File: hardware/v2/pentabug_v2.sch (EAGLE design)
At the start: 49 parts, among them IC1 ATMEGA88

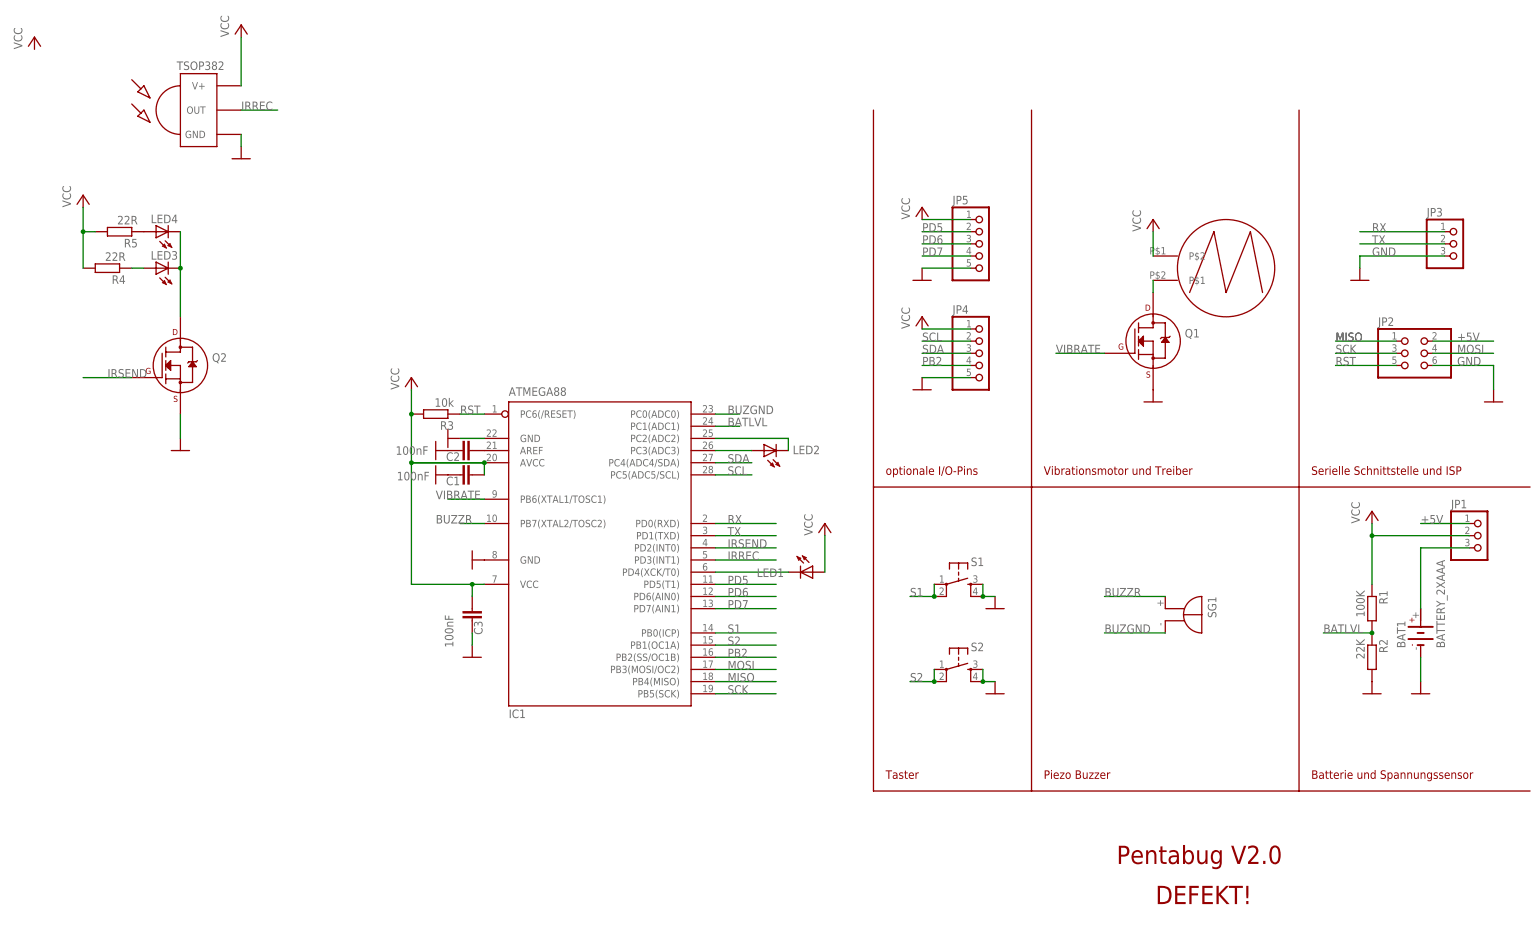
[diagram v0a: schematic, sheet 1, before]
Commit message: fixes issue #6, correct values for r4 and r5
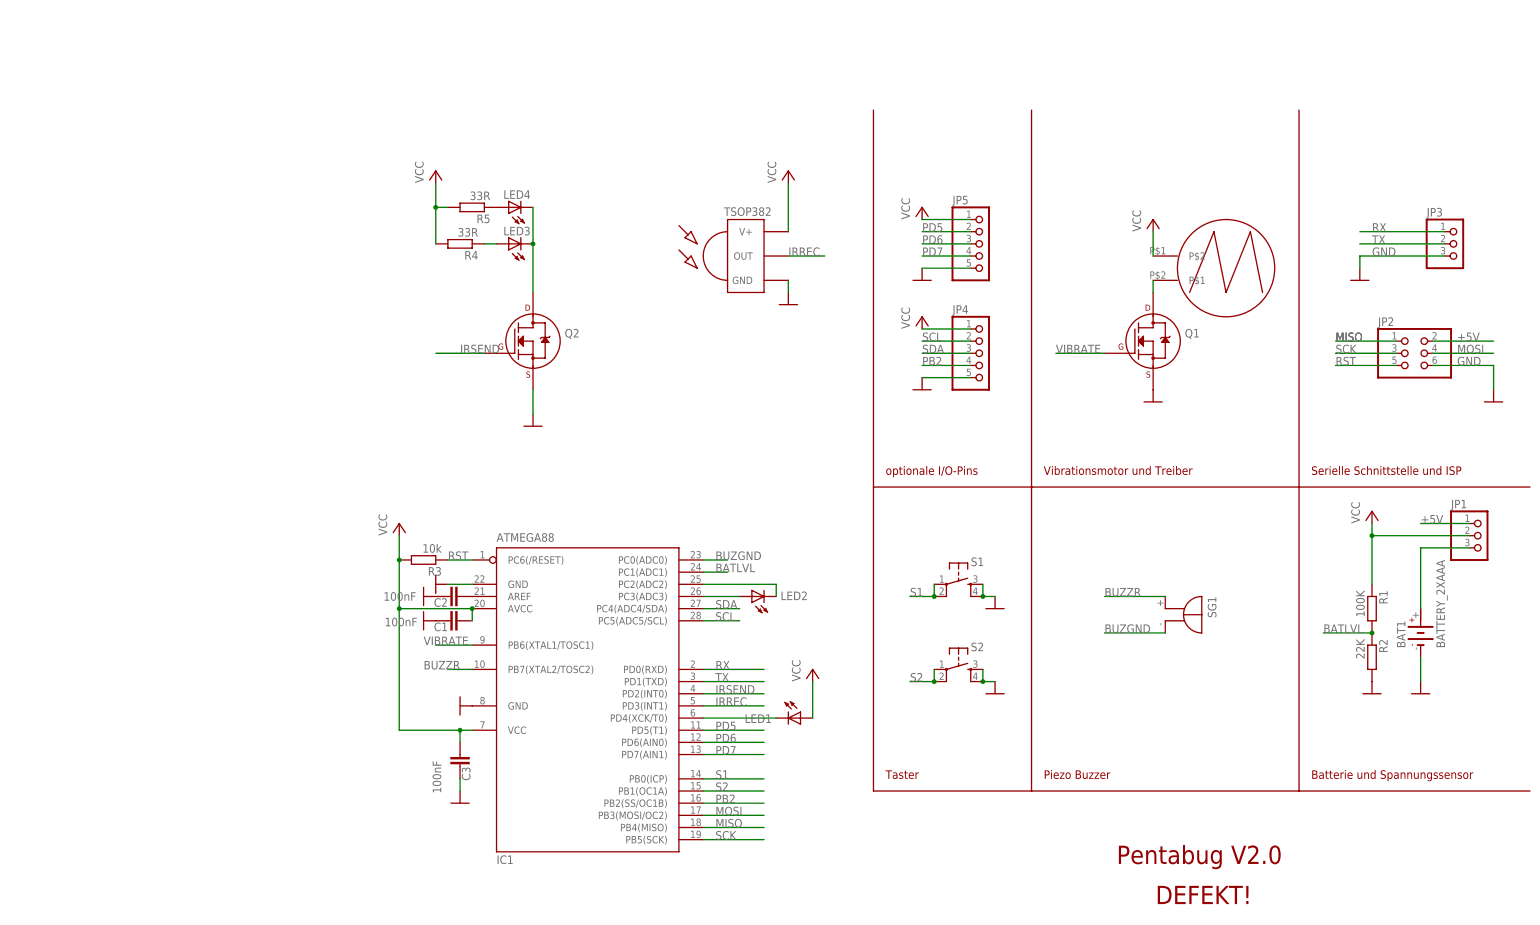
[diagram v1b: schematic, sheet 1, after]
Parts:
- R4, R5: value 22R -> 33R
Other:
- moved on the sheet: C1, C2, C3, IC1, LED1, LED2, LED3, LED4, Q2, R3, R4, R5

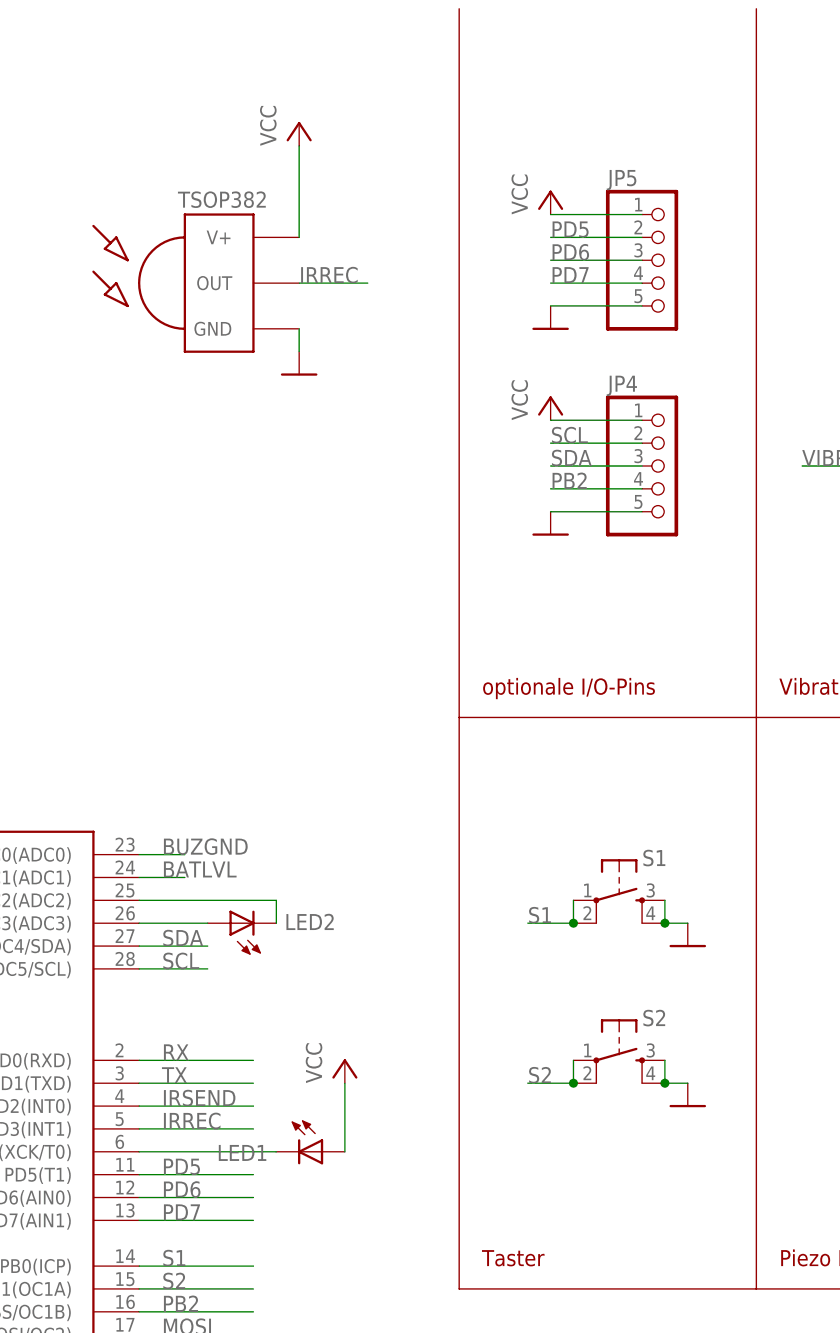
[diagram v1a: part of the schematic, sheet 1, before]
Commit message: correct labels in schematic for pentatonic fixes #7
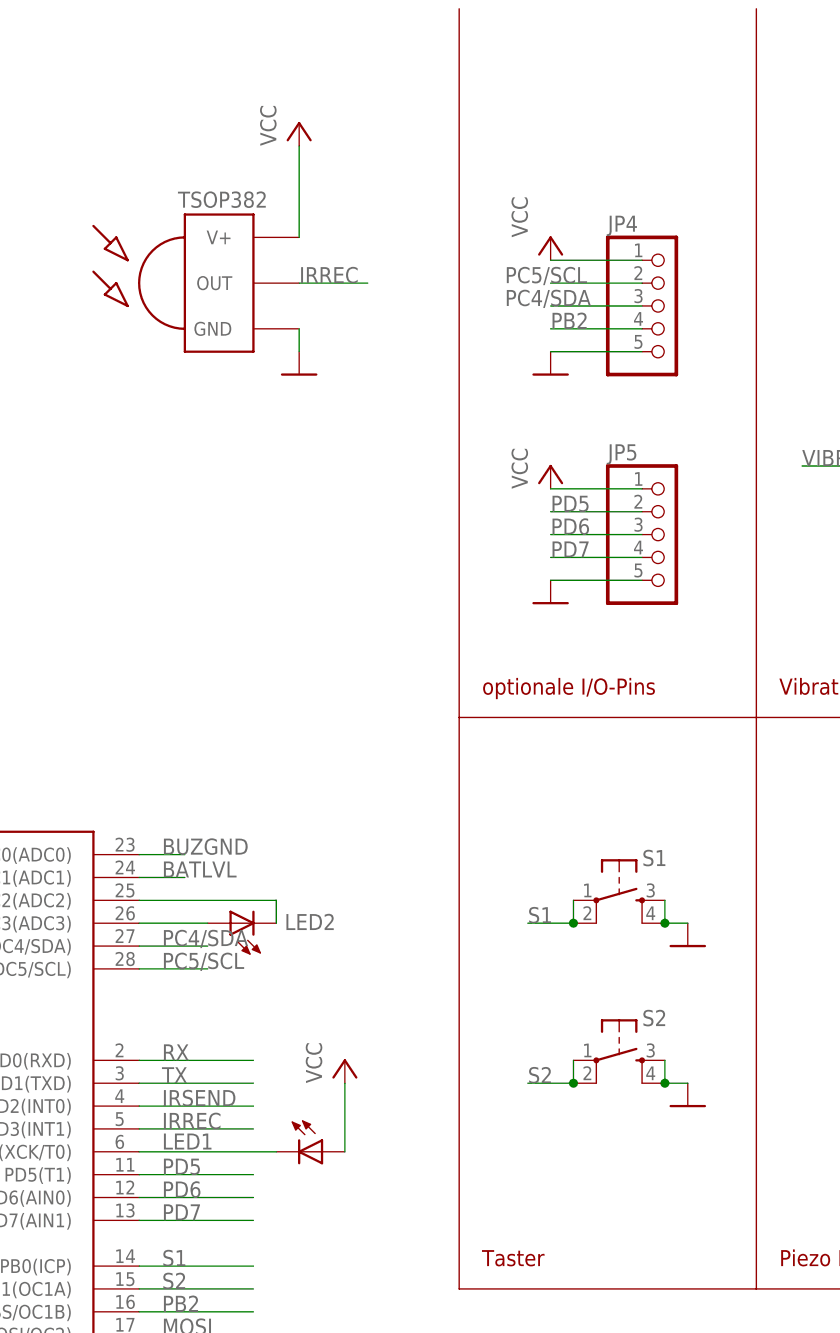
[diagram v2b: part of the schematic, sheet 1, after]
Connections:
- net PB2_T renamed PD7_T
- net SCL renamed PC5/SCL
- net SDA renamed PC4/SDA
- net PC4_T: now also LED9.C, S7.S, S7.S1, SV5.3; no longer LED6.C, S4.S, S4.S1, SV4.3
- net PC5_T: now also LED8.C, S6.S, S6.S1, SV5.2; no longer LED5.C, S3.S, S3.S1, SV4.2
- net PD5_T: now also LED5.C, S3.S, S3.S1, SV4.2; no longer LED8.C, S6.S, S6.S1, SV5.2
- net PD6_T: now also LED6.C, S4.S, S4.S1, SV4.3; no longer LED9.C, S7.S, S7.S1, SV5.3
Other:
- moved on the sheet: JP4, JP5, SV4, SV5
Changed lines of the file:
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@@
 <?xml version="1.0" encoding="utf-8"?>
 <!DOCTYPE eagle SYSTEM "eagle.dtd">
-<eagle version="6.4">
+<eagle version="6.5.0">
 <drawing>
 <settings>
@@
 <instance part="R3" gate="G$1" x="-25.4" y="25.4" rot="R180"/>
 <instance part="LED1" gate="G$1" x="53.34" y="-7.62" smashed="yes" rot="R270">
-<attribute name="NAME" x="41.656" y="-8.636" size="1.778" layer="95"/>
+<attribute name="NAME" x="35.56" y="-7.366" size="1.778" layer="95"/>
 <attribute name="VALUE" x="48.768" y="-13.335" size="1.778" layer="96"/>
 </instance>
@@
 <instance part="R2" gate="G$1" x="172.72" y="5.08" rot="R270"/>
 <instance part="GND13" gate="1" x="172.72" y="-2.54" smashed="yes"/>
-<instance part="JP5" gate="A" x="91.44" y="91.44"/>
-<instance part="JP4" gate="A" x="91.44" y="68.58"/>
-<instance part="GND14" gate="1" x="78.74" y="60.96" smashed="yes"/>
-<instance part="GND15" gate="1" x="78.74" y="83.82" smashed="yes"/>
-<instance part="P+4" gate="VCC" x="78.74" y="76.2"/>
-<instance part="P+6" gate="VCC" x="78.74" y="99.06"/>
+<instance part="JP5" gate="A" x="91.44" y="60.96"/>
+<instance part="JP4" gate="A" x="91.44" y="86.36"/>
+<instance part="GND14" gate="1" x="78.74" y="78.74" smashed="yes"/>
+<instance part="GND15" gate="1" x="78.74" y="53.34" smashed="yes"/>
+<instance part="P+4" gate="VCC" x="78.74" y="93.98" smashed="yes">
+<attribute name="VALUE" x="76.2" y="93.98" size="1.778" layer="96" rot="R90"/>
+</instance>
+<instance part="P+6" gate="VCC" x="78.74" y="68.58" smashed="yes">
+<attribute name="VALUE" x="76.2" y="66.04" size="1.778" layer="96" rot="R90"/>
+</instance>
 <instance part="JP1" gate="A" x="195.58" y="30.48"/>
 <instance part="Q2" gate="G$1" x="-2.54" y="71.12"/>
@@
 <segment>
 <pinref part="JP5" gate="A" pin="2"/>
-<wire x1="88.9" y1="93.98" x2="78.74" y2="93.98" width="0.1524" layer="91"/>
-<label x="78.74" y="93.98" size="1.778" layer="95"/>
+<wire x1="88.9" y1="63.5" x2="78.74" y2="63.5" width="0.1524" layer="91"/>
+<label x="78.74" y="63.5" size="1.778" layer="95"/>
 </segment>
 </net>
@@
 <pinref part="JP4" gate="A" pin="1"/>
 <pinref part="P+4" gate="VCC" pin="VCC"/>
-<wire x1="78.74" y1="73.66" x2="88.9" y2="73.66" width="0.1524" layer="91"/>
+<wire x1="78.74" y1="91.44" x2="88.9" y2="91.44" width="0.1524" layer="91"/>
 </segment>
 <segment>
 <pinref part="JP5" gate="A" pin="1"/>
 <pinref part="P+6" gate="VCC" pin="VCC"/>
-<wire x1="78.74" y1="96.52" x2="88.9" y2="96.52" width="0.1524" layer="91"/>
+<wire x1="78.74" y1="66.04" x2="88.9" y2="66.04" width="0.1524" layer="91"/>
 </segment>
 <segment>
@@
 <pinref part="JP5" gate="A" pin="5"/>
 <pinref part="GND15" gate="1" pin="GND"/>
-<wire x1="78.74" y1="86.36" x2="88.9" y2="86.36" width="0.1524" layer="91"/>
+<wire x1="78.74" y1="55.88" x2="88.9" y2="55.88" width="0.1524" layer="91"/>
 </segment>
 <segment>
@@
 <pinref part="JP4" gate="A" pin="5"/>
 <pinref part="GND14" gate="1" pin="GND"/>
-<wire x1="78.74" y1="63.5" x2="88.9" y2="63.5" width="0.1524" layer="91"/>
+<wire x1="78.74" y1="81.28" x2="88.9" y2="81.28" width="0.1524" layer="91"/>
 </segment>
 </net>
@@
 <segment>
 <pinref part="JP5" gate="A" pin="3"/>
-<wire x1="88.9" y1="91.44" x2="78.74" y2="91.44" width="0.1524" layer="91"/>
-<label x="78.74" y="91.44" size="1.778" layer="95"/>
+<wire x1="88.9" y1="60.96" x2="78.74" y2="60.96" width="0.1524" layer="91"/>
+<label x="78.74" y="60.96" size="1.778" layer="95"/>
 </segment>
 </net>
@@
 </segment>
 </net>
-<net name="SCL" class="0">
+<net name="PC5/SCL" class="0">
 <segment>
 <pinref part="JP4" gate="A" pin="2"/>
-<wire x1="88.9" y1="71.12" x2="78.74" y2="71.12" width="0.1524" layer="91"/>
-<label x="78.74" y="71.12" size="1.778" layer="95"/>
+<wire x1="88.9" y1="88.9" x2="78.74" y2="88.9" width="0.1524" layer="91"/>
+<label x="73.66" y="88.9" size="1.778" layer="95"/>
 </segment>
 <segment>
@@
 </segment>
 </net>
-<net name="SDA" class="0">
+<net name="PC4/SDA" class="0">
 <segment>
 <pinref part="JP4" gate="A" pin="3"/>
-<wire x1="88.9" y1="68.58" x2="78.74" y2="68.58" width="0.1524" layer="91"/>
-<label x="78.74" y="68.58" size="1.778" layer="95"/>
+<wire x1="88.9" y1="86.36" x2="78.74" y2="86.36" width="0.1524" layer="91"/>
+<label x="73.66" y="86.36" size="1.778" layer="95"/>
 </segment>
 <segment>
@@
 <segment>
 <pinref part="JP4" gate="A" pin="4"/>
-<wire x1="88.9" y1="66.04" x2="78.74" y2="66.04" width="0.1524" layer="91"/>
-<label x="78.74" y="66.04" size="1.778" layer="95"/>
+<wire x1="88.9" y1="83.82" x2="78.74" y2="83.82" width="0.1524" layer="91"/>
+<label x="78.74" y="83.82" size="1.778" layer="95"/>
 </segment>
 </net>
@@
 <segment>
 <pinref part="JP5" gate="A" pin="4"/>
-<wire x1="88.9" y1="88.9" x2="78.74" y2="88.9" width="0.1524" layer="91"/>
-<label x="78.74" y="88.9" size="1.778" layer="95"/>
+<wire x1="88.9" y1="58.42" x2="78.74" y2="58.42" width="0.1524" layer="91"/>
+<label x="78.74" y="58.42" size="1.778" layer="95"/>
 </segment>
 </net>
@@
 </plain>
 <instances>
-<instance part="SV4" gate="G$1" x="35.56" y="63.5" rot="MR180"/>
-<instance part="SV5" gate="G$1" x="35.56" y="27.94" rot="MR180"/>
-<instance part="P+11" gate="VCC" x="43.18" y="35.56"/>
-<instance part="GND17" gate="1" x="50.8" y="55.88"/>
-<instance part="GND18" gate="1" x="48.26" y="20.32"/>
+<instance part="SV4" gate="G$1" x="35.56" y="33.02" rot="MR180"/>
+<instance part="SV5" gate="G$1" x="35.56" y="63.5" rot="MR180"/>
+<instance part="P+11" gate="VCC" x="48.26" y="71.12"/>
+<instance part="GND17" gate="1" x="50.8" y="25.4"/>
+<instance part="GND18" gate="1" x="48.26" y="55.88"/>
 <instance part="LED5" gate="G$1" x="81.28" y="58.42"/>
 <instance part="S3" gate="1" x="78.74" y="43.18"/>
@@
 <pinref part="SV5" gate="G$1" pin="1"/>
 <pinref part="P+11" gate="VCC" pin="VCC"/>
+<wire x1="48.26" y1="68.58" x2="43.18" y2="68.58" width="0.1524" layer="91"/>
 </segment>
 <segment>
@@
 <pinref part="SV4" gate="G$1" pin="5"/>
 <pinref part="GND17" gate="1" pin="GND"/>
-<wire x1="50.8" y1="58.42" x2="43.18" y2="58.42" width="0.1524" layer="91"/>
+<wire x1="50.8" y1="27.94" x2="43.18" y2="27.94" width="0.1524" layer="91"/>
 </segment>
 <segment>
 <pinref part="SV5" gate="G$1" pin="5"/>
 <pinref part="GND18" gate="1" pin="GND"/>
-<wire x1="48.26" y1="22.86" x2="43.18" y2="22.86" width="0.1524" layer="91"/>
+<wire x1="48.26" y1="58.42" x2="43.18" y2="58.42" width="0.1524" layer="91"/>
 </segment>
 <segment>
@@
 </segment>
 </net>
-<net name="PC5_T" class="0">
+<net name="PD5_T" class="0">
 <segment>
 <pinref part="SV4" gate="G$1" pin="2"/>
-<wire x1="43.18" y1="66.04" x2="53.34" y2="66.04" width="0.1524" layer="91"/>
-<label x="48.26" y="66.04" size="1.778" layer="95"/>
+<wire x1="43.18" y1="35.56" x2="53.34" y2="35.56" width="0.1524" layer="91"/>
+<label x="48.26" y="35.56" size="1.778" layer="95"/>
 </segment>
 <segment>
@@
 </segment>
 </net>
-<net name="PC4_T" class="0">
+<net name="PD6_T" class="0">
 <segment>
 <pinref part="SV4" gate="G$1" pin="3"/>
-<wire x1="43.18" y1="63.5" x2="53.34" y2="63.5" width="0.1524" layer="91"/>
-<label x="48.26" y="63.5" size="1.778" layer="95"/>
+<wire x1="43.18" y1="33.02" x2="53.34" y2="33.02" width="0.1524" layer="91"/>
+<label x="48.26" y="33.02" size="1.778" layer="95"/>
 </segment>
 <segment>
@@
 </segment>
 </net>
-<net name="PD5_T" class="0">
+<net name="PC5_T" class="0">
 <segment>
 <pinref part="SV5" gate="G$1" pin="2"/>
-<wire x1="43.18" y1="30.48" x2="53.34" y2="30.48" width="0.1524" layer="91"/>
-<label x="48.26" y="30.48" size="1.778" layer="95"/>
+<wire x1="43.18" y1="66.04" x2="53.34" y2="66.04" width="0.1524" layer="91"/>
+<label x="48.26" y="66.04" size="1.778" layer="95"/>
 </segment>
 <segment>
@@
 </segment>
 </net>
-<net name="PD6_T" class="0">
+<net name="PC4_T" class="0">
 <segment>
 <pinref part="SV5" gate="G$1" pin="3"/>
-<wire x1="43.18" y1="27.94" x2="53.34" y2="27.94" width="0.1524" layer="91"/>
-<label x="48.26" y="27.94" size="1.778" layer="95"/>
+<wire x1="43.18" y1="63.5" x2="53.34" y2="63.5" width="0.1524" layer="91"/>
+<label x="48.26" y="63.5" size="1.778" layer="95"/>
 </segment>
 <segment>
@@
 </segment>
 </net>
-<net name="PB2_T" class="0">
+<net name="PD7_T" class="0">
 <segment>
 <pinref part="SV4" gate="G$1" pin="4"/>
-<wire x1="43.18" y1="60.96" x2="53.34" y2="60.96" width="0.1524" layer="91"/>
-<label x="48.26" y="60.96" size="1.778" layer="95"/>
-</segment>
-<segment>
+<wire x1="43.18" y1="30.48" x2="53.34" y2="30.48" width="0.1524" layer="91"/>
+<label x="48.26" y="30.48" size="1.778" layer="95"/>
+</segment>
+<segment>
